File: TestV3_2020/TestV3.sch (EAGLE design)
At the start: 46 parts, among them IC1 MCP1703T-3302E/CB, IC2 MCP1703T-3302E/CB, J3 USB_B_PTH, Q1 NPN-BJT, Q2 NPN-BJT, U2 MP2451

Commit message: minor change
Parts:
- removed C1: 100uF, SparkFun3:CAP_POL1206
- removed C2, C3: 10uF, SparkFun2:CAP0805
- removed D2: (no value), SparkFun3:DIODESOD
- removed IC1, IC2: MCP1703T-3302E/CB, okie:MCP1700T
- removed U4: (no value), JH:TPS54X0
- added 2C5, 2C6: 4.7uF, SparkFun-Capacitors:4.7UF-0603-6.3V-(10%)
- added 2C7: 10nF, SparkFun-Capacitors:10NF-0603-50V-10%
- added 2C8: 22UF, SparkFun-Capacitors:22UF-1210-16V-20%
- added U1: (no value), JH:TPS54X31
- L1: value ferrite bead -> 6.8uH; device SparkFun3:INDUCTOR0603 -> JH:INDUCTORSWPA8040
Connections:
- net 12V: no longer C1.+, D2.C, IC1.VIN, IC2.VIN
- net 3.3V: now also 2L1.2; no longer 2L1.1
- net AV-: no longer C3.2, IC2.GND, L1.1
- net GND: no longer C1.-, C2.2, IC1.GND, L1.2
- net N$5: now also 2L1.1; no longer 2L1.2
- net VCC: no longer C2.1, IC1.VOUT
- net VCCA: no longer C3.1, IC2.VOUT
- net V_USB: no longer D2.A
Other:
- moved on the sheet: 2L1

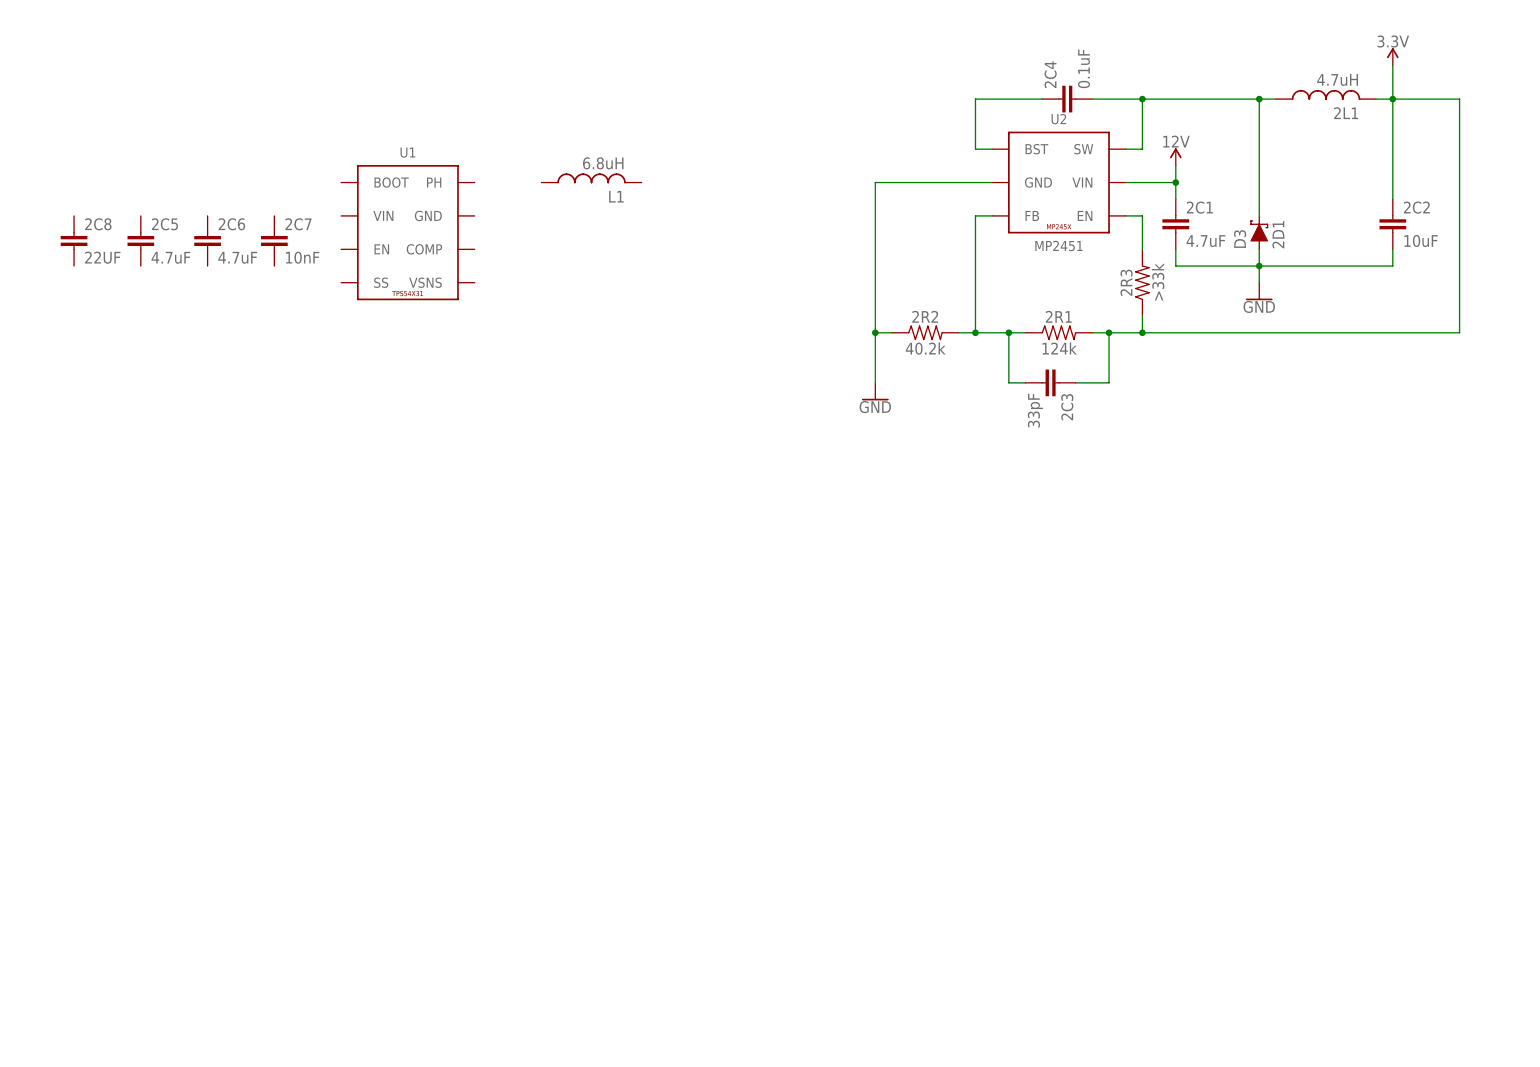
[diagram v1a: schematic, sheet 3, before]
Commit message: Finished schematic of buck converters will make changes to the values of compensation components to make them more standard values
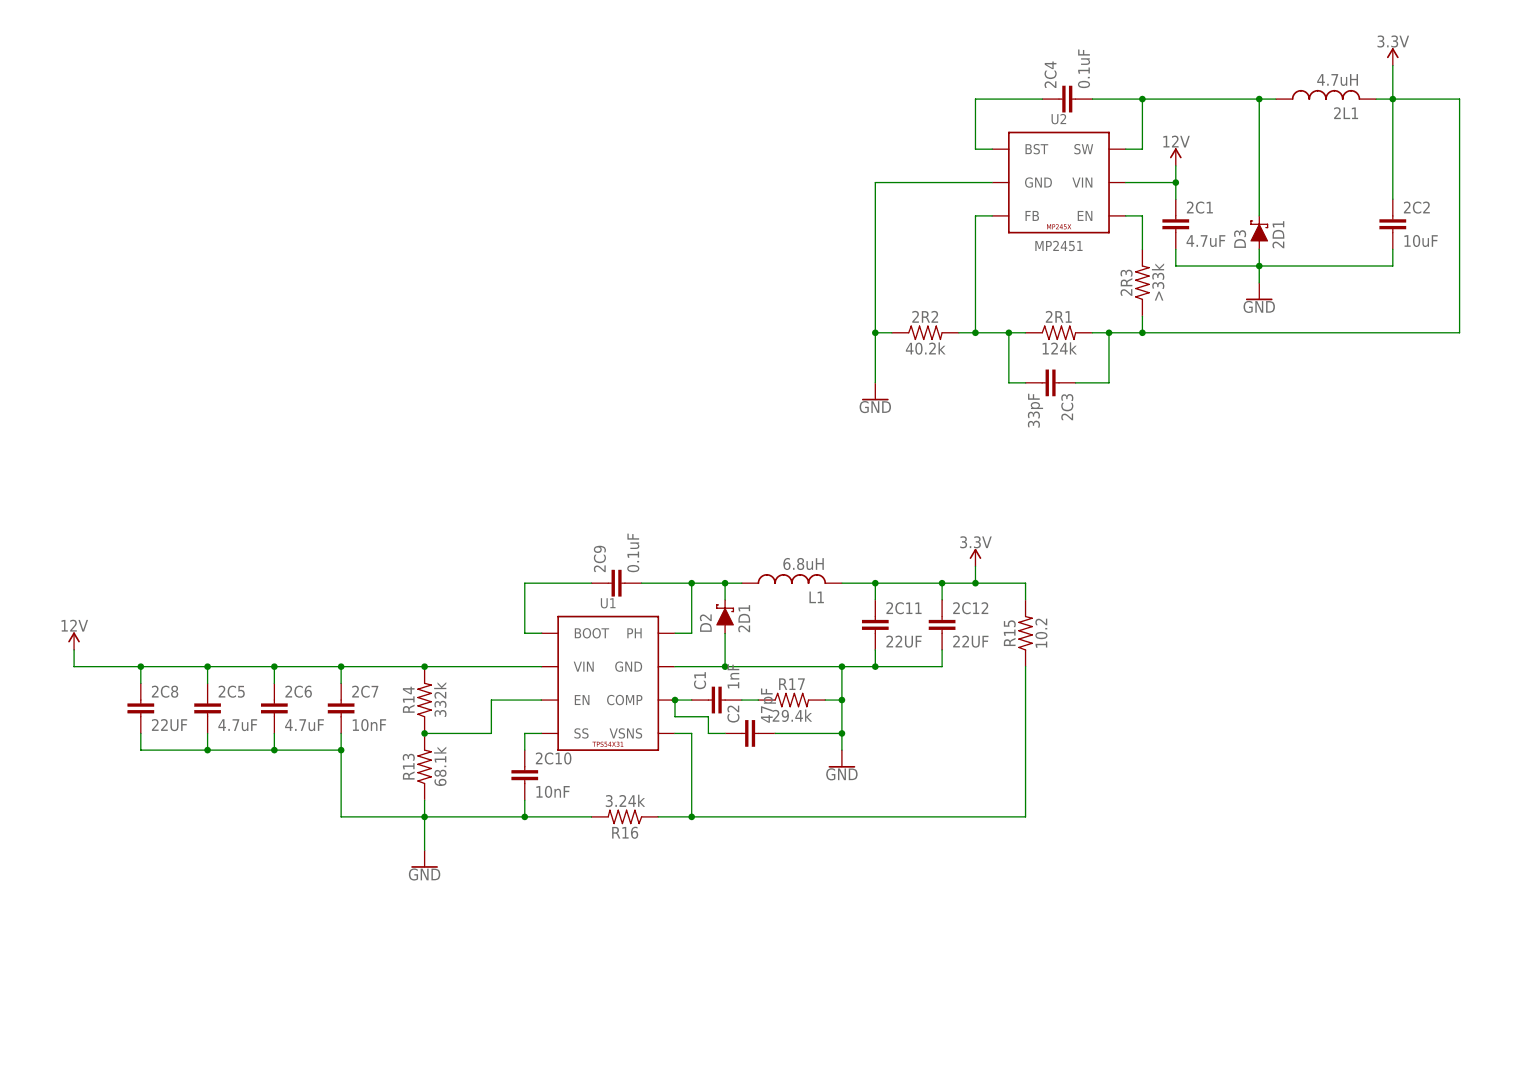
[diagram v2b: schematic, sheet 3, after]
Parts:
- added 2C10: 10nF, SparkFun-Capacitors:10NF-0603-50V-10%
- added 2C11, 2C12: 22UF, SparkFun-Capacitors:22UF-1210-16V-20%
- added 2C9: 0.1uF, SparkFun-Capacitors:0.1UF-0603-25V-5%
- added C1: 1nF, SparkFun-Capacitors:1.0NF/1000PF-0603-50V-10%
- added C2: 47pF, SparkFun-Capacitors:47PF-0603-50V-5%
- added D2: 2D1, SparkFun-DiscreteSemi:DIODE-SCHOTTKY-SS14
- added R13: 68.1k, SparkFun-Resistors:68.1KOHM-0603-1/10W-1%
- added R14: 332k, SparkFun-Resistors:RESISTOR0603
- added R15: 10.2, SparkFun-Resistors:RESISTOR0603
- added R16: 3.24k, SparkFun-Resistors:RESISTOR0603
- added R17: 29.4k, SparkFun-Resistors:RESISTOR0603
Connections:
- new net N$10: 2C9.2, D2.C, L1.1, U1.PH
- new net N$11: R13.2, R14.1, U1.EN
- new net N$12: C1.2, R17.1
- new net N$13: R15.1, R16.1, U1.VSNS
- new net N$14: C1.1, C2.1, U1.COMP
- new net N$8: 2C10.1, U1.SS
- new net N$9: 2C9.1, U1.BOOT
- net 12V: now also 2C5.1, 2C6.1, 2C7.1, 2C8.1, R14.2, U1.VIN
- net 3.3V: now also 2C11.1, 2C12.1, L1.2, R15.2
- net GND: now also 2C10.2, 2C11.2, 2C12.2, 2C5.2, 2C6.2, 2C7.2, 2C8.2, C2.2, D2.A, R13.1, R16.2, R17.2, U1.GND
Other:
- moved on the sheet: 2C5, 2C6, 2C7, 2C8, L1, U1

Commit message: shift buck converters to own library rcl
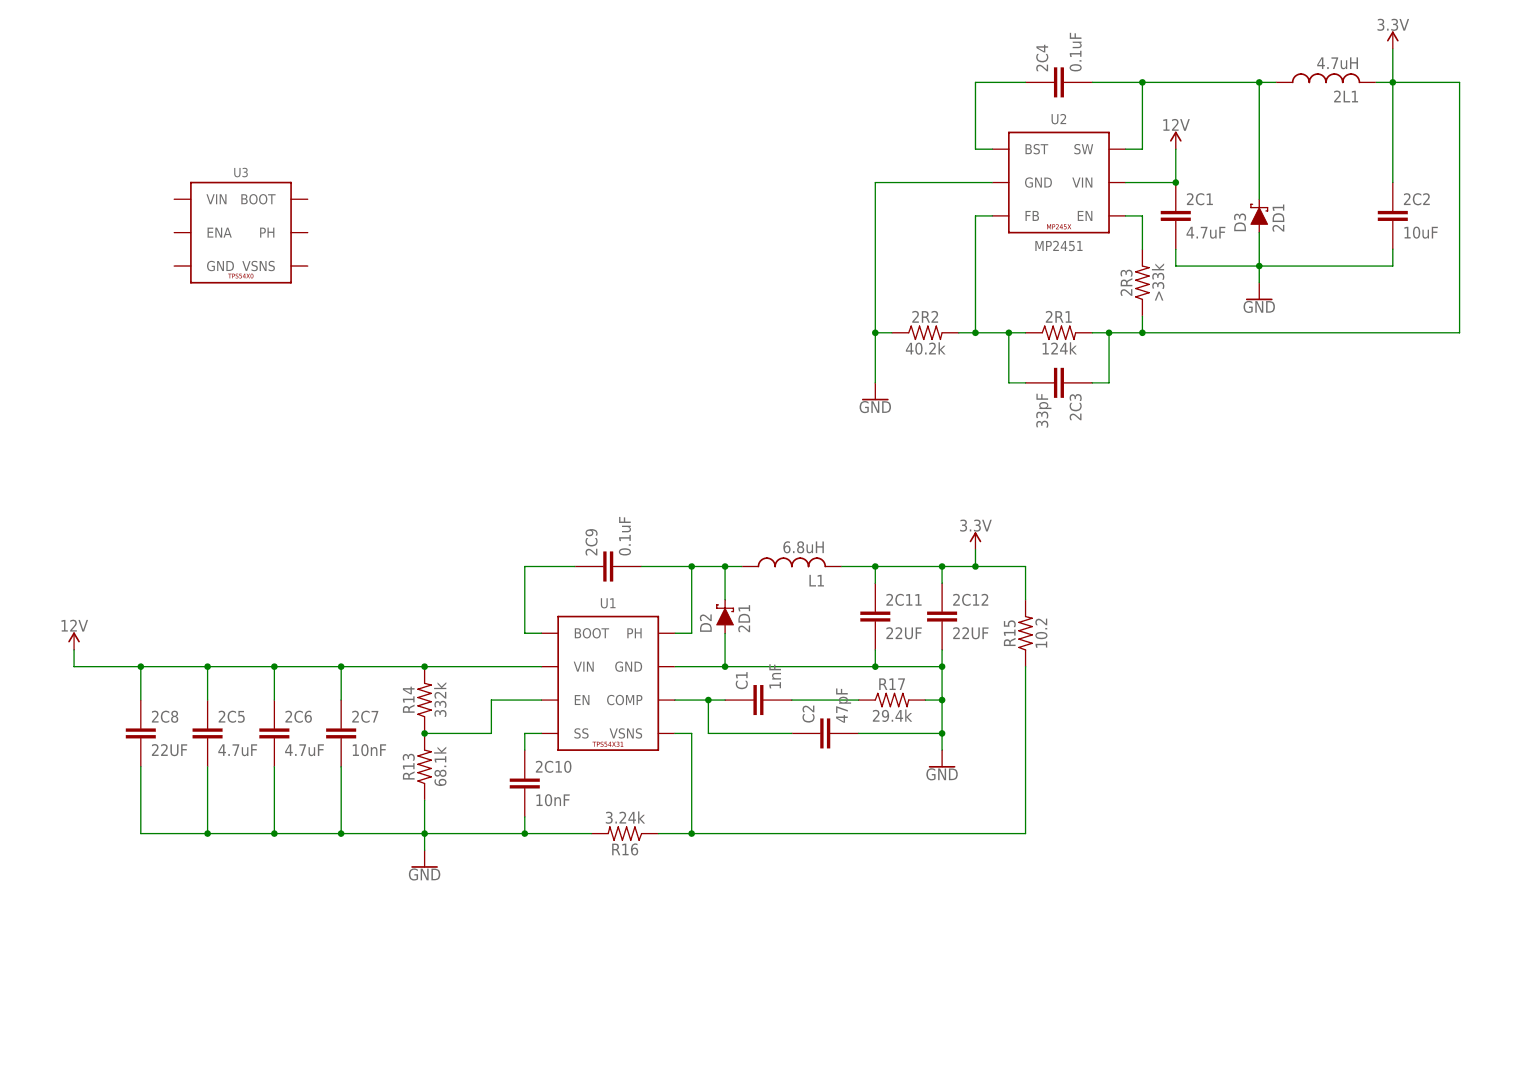
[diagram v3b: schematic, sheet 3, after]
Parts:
- added U3: (no value), JH:TPS54X0
- 2C1, 2C5, 2C6: device SparkFun-Capacitors:4.7UF-0603-6.3V-(10%) -> JH:CAPACITOR0603
- 2C10, 2C7: device SparkFun-Capacitors:10NF-0603-50V-10% -> JH:CAPACITOR0603
- 2C11, 2C12, 2C8: device SparkFun-Capacitors:22UF-1210-16V-20% -> JH:CAPACITOR1210
- 2C2: device SparkFun-Capacitors:10UF-0603-6.3V-20% -> JH:CAPACITOR0603
- 2C3: device SparkFun-Capacitors:33PF-0603-50V-5% -> JH:CAPACITOR0603
- 2C4, 2C9: device SparkFun-Capacitors:0.1UF-0603-25V-5% -> JH:CAPACITOR0603
- 2R1, 2R2, 2R3, R14, R15, R16, R17: device SparkFun-Resistors:RESISTOR0603 -> JH:RESISTOR0603
- C1: device SparkFun-Capacitors:1.0NF/1000PF-0603-50V-10% -> JH:CAPACITOR0603
- C2: device SparkFun-Capacitors:47PF-0603-50V-5% -> JH:CAPACITOR0603
- R13: device SparkFun-Resistors:68.1KOHM-0603-1/10W-1% -> JH:RESISTOR0603
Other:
- moved on the sheet: 2L1, D3, L1, R16, R17

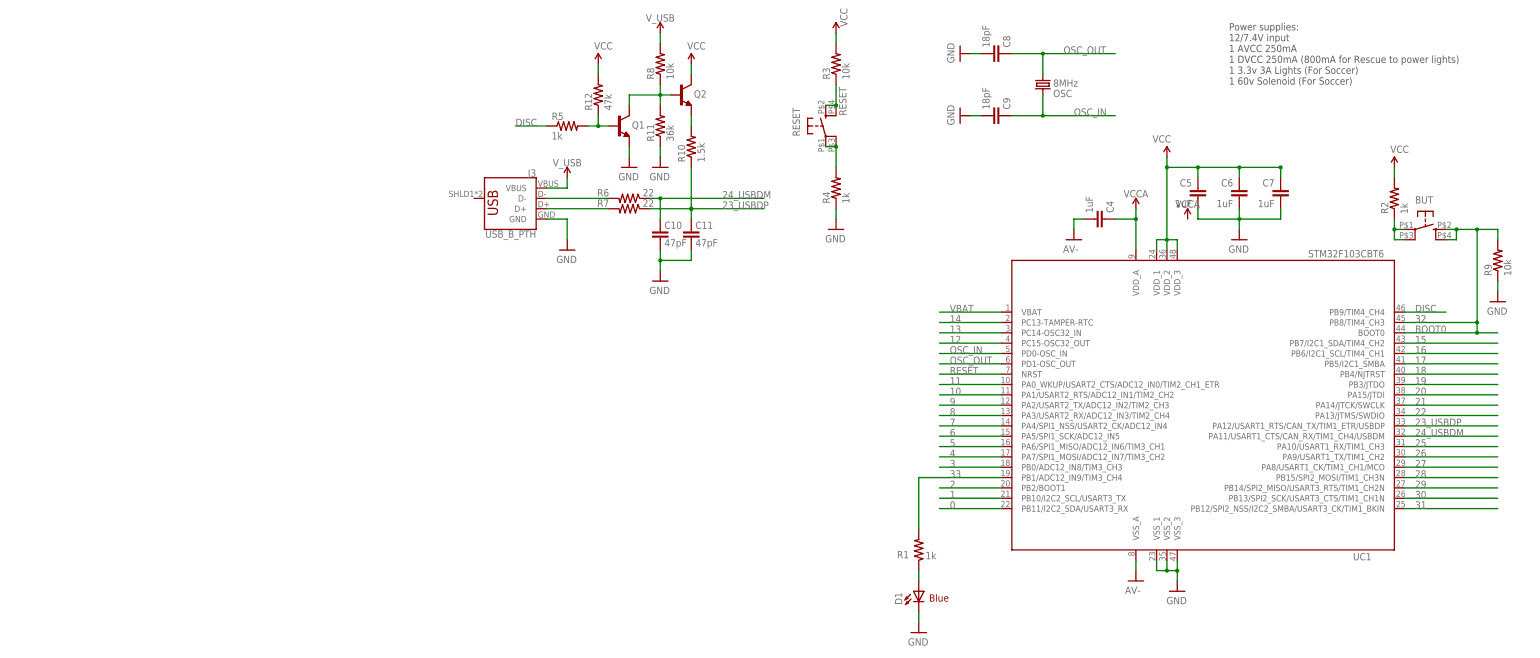
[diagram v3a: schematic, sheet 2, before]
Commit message: Added Datasheets folder and cleaned up the schematic to use less random libraries
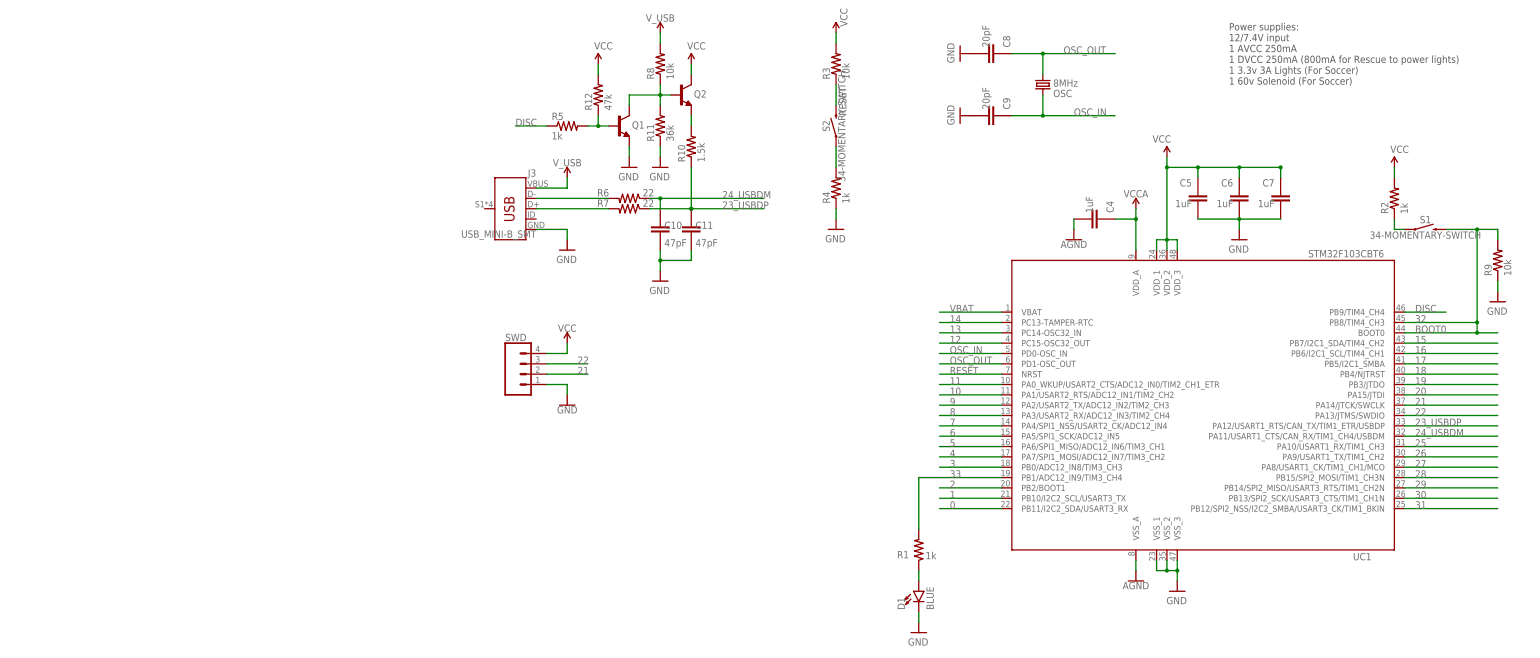
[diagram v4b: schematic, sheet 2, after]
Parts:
- removed BUT, RESET: KMR211GLFS, okie:BUTTON-KMR241GLFS
- removed U3: (no value), JH:TPS54X0
- added S1, S2: 34-MOMENTARY-SWITCH, JH:34-MOMENTARY-SWITCH
- added SWD: (no value), SparkFun-Connectors:CONN_04LOCK
- 2C11, 2C12: value 22UF -> 47uF
- C10, C11, C4, C5, C6, C7: device SparkFun:CAP0402 -> JH:CAPACITOR0603
- C8, C9: value 18pF -> 20pF; device SparkFun:CAP0402 -> JH:CAPACITOR0603
- D1: value Blue -> BLUE; device SparkFun:LED1206 -> SparkFun-LED:LED-BLUE0603
- D2, D3: value 2D1 -> SS34
- J3: value USB_B_PTH -> USB_MINI-B_SMT; device SparkFun-Connectors:USB_B_PTH -> SparkFun-Connectors:USB_MINI-B_SMT
- OSC: device SparkFun2:CRYSTAL5X3 -> SparkFun-Clocks:CRYSTALSMD-5X3.2-2PAD
- Q1, Q2: value NPN-BJT -> 600mA/40V; device SparkFun2:TRANSISTOR_NPNSOT23 -> SparkFun-DiscreteSemi:TRANS_NPN-MMBT2222AL
- R1, R10, R11, R12, R2, R3, R4, R5, R6, R7, R8, R9: device SparkFun:RESISTOR0402 -> JH:RESISTOR0603
- R15: value 10.2 -> 10k
- UC1: device stm32:STM32F103CB -> JH:STM32F103CBT6
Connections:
- net AV- renamed AGND
- net 21: now also SWD.2
- net 22: now also SWD.3
- net 32: now also S1.2; no longer BUT.2, BUT.4
- net GND: now also SWD.1
- net N$1: now also S1.1; no longer BUT.1, BUT.3
- net N$4: now also S2.1; no longer RESET.1, RESET.3
- net RESET: now also S2.2; no longer RESET.2, RESET.4
- net VCC: now also SWD.4
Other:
- note added: "Change COMP and VSNS if changing to 5v"
- note removed: "Blue"
- moved on the sheet: R13, R14
